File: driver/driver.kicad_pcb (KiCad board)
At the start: 2 copper layers, 59 parts, among them J1 BARREL_JACK, J2 CONN_02X32, Q1 DUAL_NPN_MOSFET, Q10 DUAL_NPN_MOSFET, Q11 DUAL_NPN_MOSFET, Q12 DUAL_NPN_MOSFET, Q13 DUAL_NPN_MOSFET, Q14 DUAL_NPN_MOSFET, Q15 DUAL_NPN_MOSFET, Q16 DUAL_NPN_MOSFET, Q17 DUAL_NPN_MOSFET, Q18 DUAL_NPN_MOSFET, Q19 DUAL_NPN_MOSFET, Q2 DUAL_NPN_MOSFET, Q20 DUAL_NPN_MOSFET, Q21 DUAL_NPN_MOSFET, Q22 DUAL_NPN_MOSFET, Q23 DUAL_NPN_MOSFET, Q24 DUAL_NPN_MOSFET, Q25 DUAL_NPN_MOSFET, Q26 DUAL_NPN_MOSFET, Q27 DUAL_NPN_MOSFET, Q28 DUAL_NPN_MOSFET, Q29 DUAL_NPN_MOSFET, Q3 DUAL_NPN_MOSFET, Q30 DUAL_NPN_MOSFET, Q31 DUAL_NPN_MOSFET, Q32 DUAL_NPN_MOSFET, Q33 DUAL_NPN_MOSFET, Q34 DUAL_NPN_MOSFET, Q35 DUAL_NPN_MOSFET, Q36 DUAL_NPN_MOSFET, Q37 DUAL_NPN_MOSFET, Q38 DUAL_NPN_MOSFET, Q39 DUAL_NPN_MOSFET, Q4 DUAL_NPN_MOSFET, Q40 DUAL_NPN_MOSFET, Q41 DUAL_NPN_MOSFET, Q42 DUAL_NPN_MOSFET, Q43 DUAL_NPN_MOSFET, Q44 DUAL_NPN_MOSFET, Q5 DUAL_NPN_MOSFET, Q6 DUAL_NPN_MOSFET, Q7 DUAL_NPN_MOSFET, Q8 DUAL_NPN_MOSFET, Q9 DUAL_NPN_MOSFET, U1 MCP23017, U2 Teensy3.2, U3 MCP23017, U4 LM7815CT, U5 MCP23017, U6 LF50ABDT-TR, U7 MCP23017, U8 MCP23017, U9 MCP23017

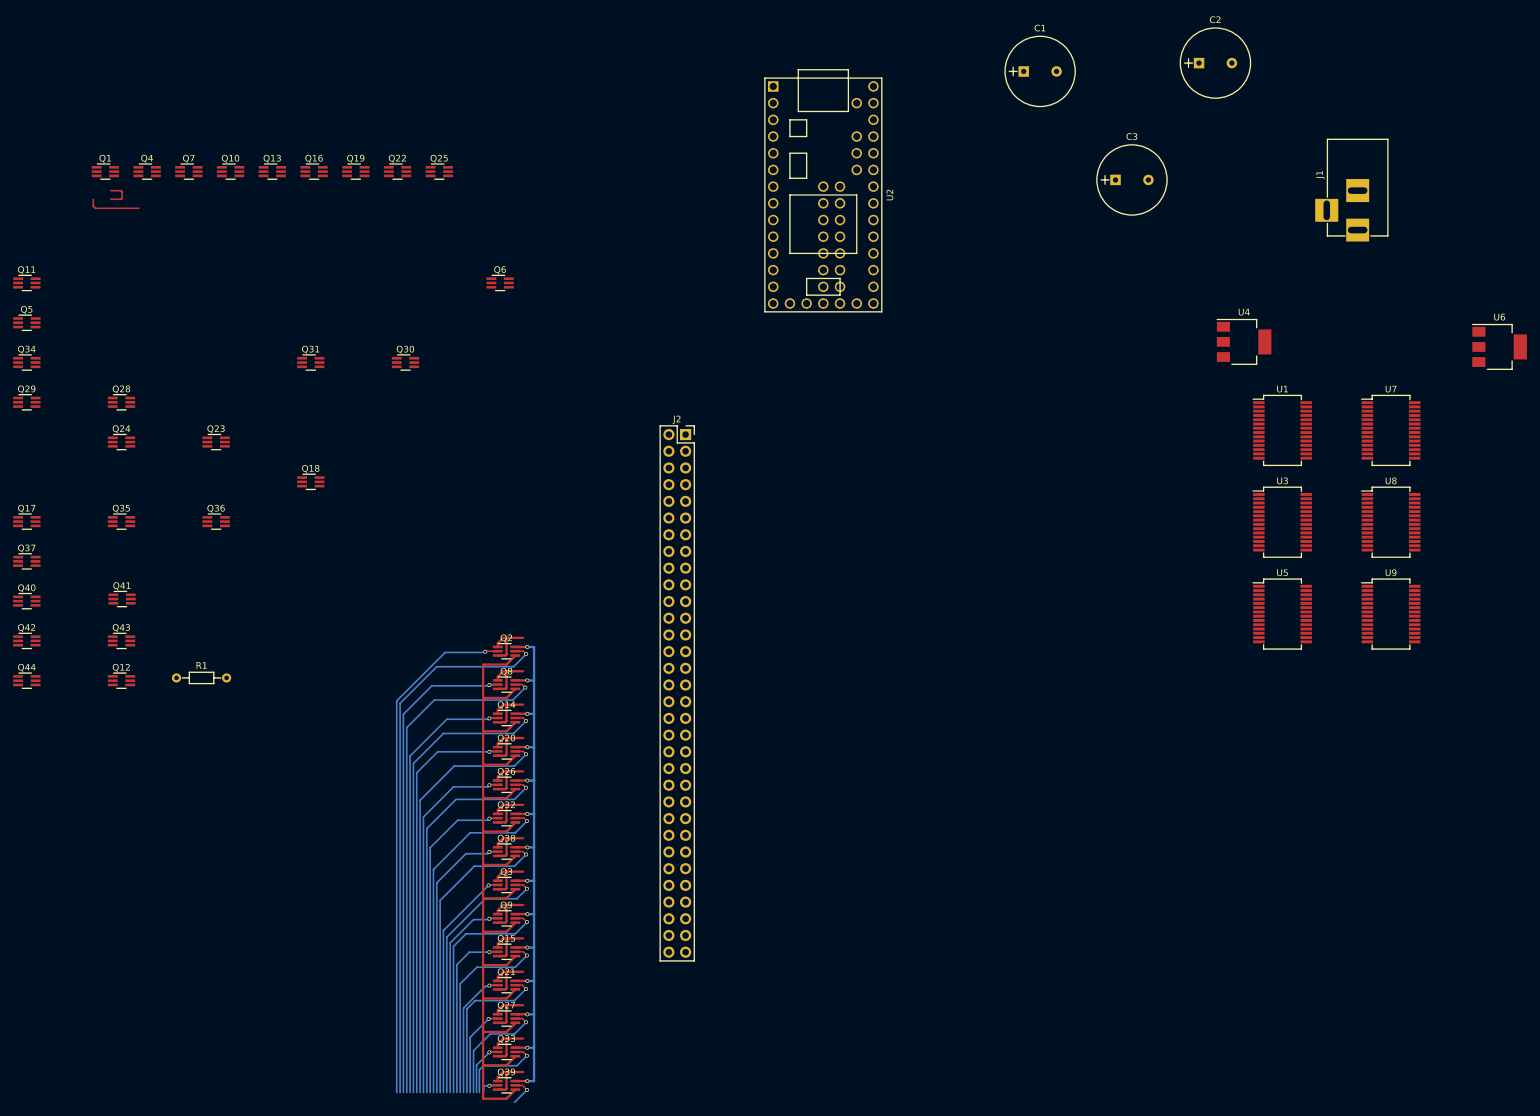
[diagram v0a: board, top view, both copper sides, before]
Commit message: layout 2nd transistor array
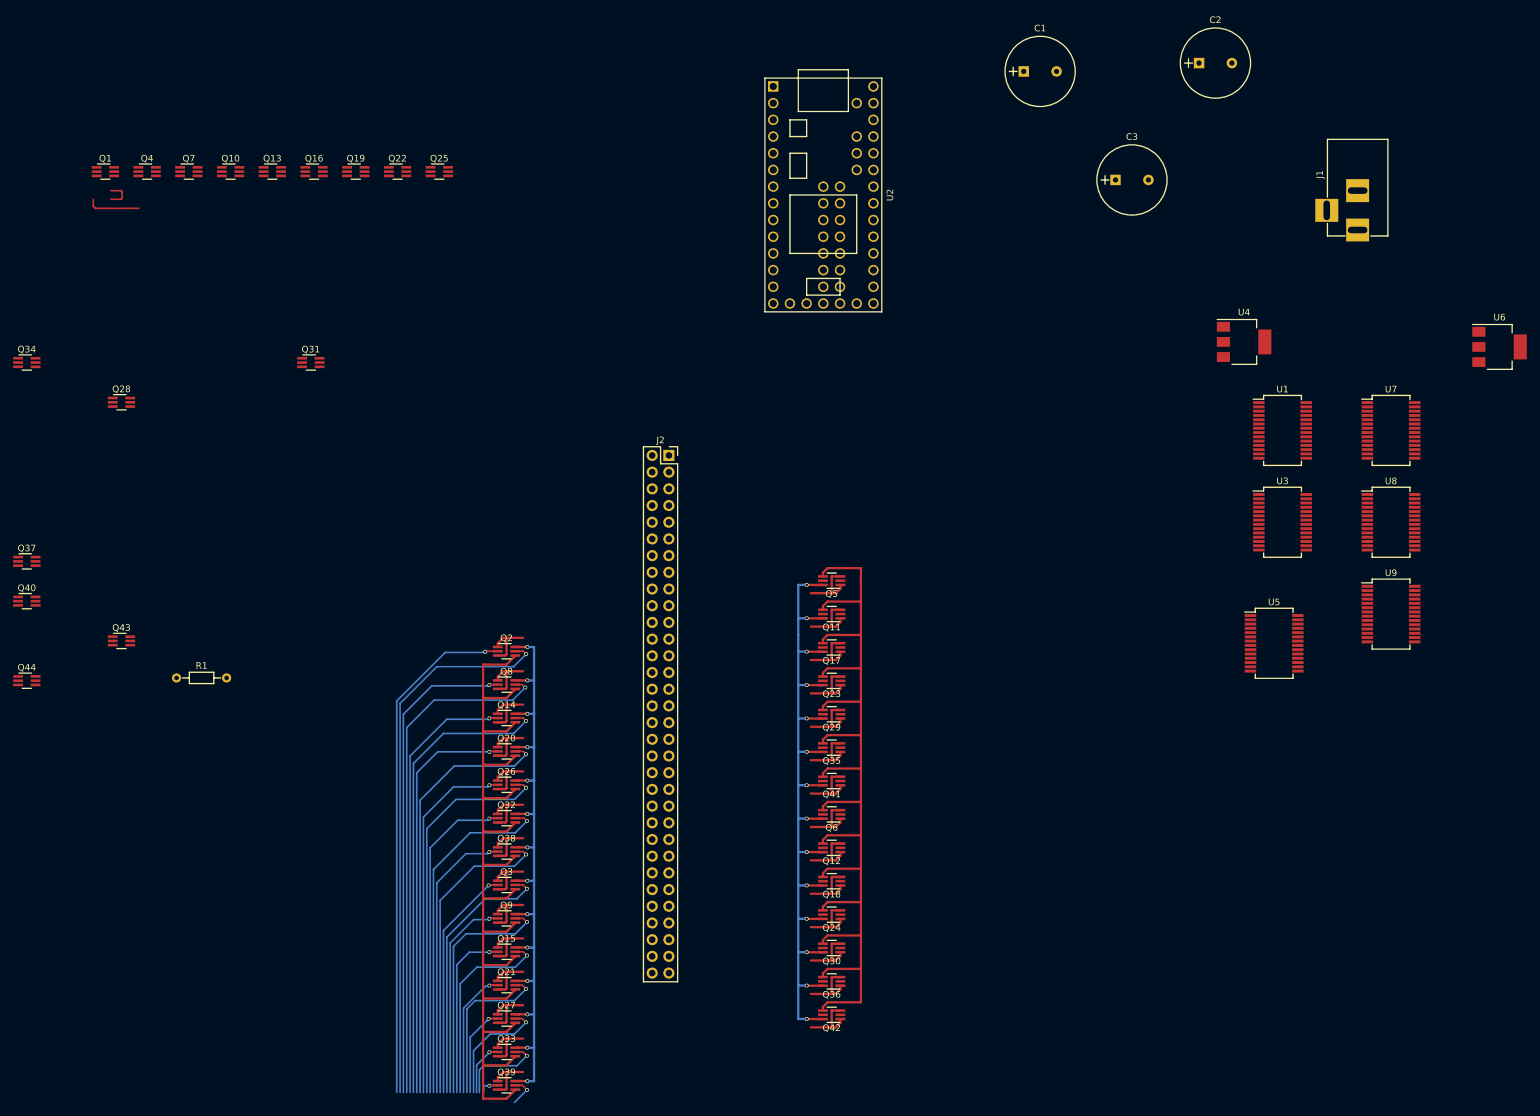
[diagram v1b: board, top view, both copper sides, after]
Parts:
- moved Q42 135.0 mm to (171.4, 168.9), turned to 180 degrees
- moved Q11 132.4 mm to (171.4, 108.0), turned to 180 degrees
- moved Q29 131.3 mm to (171.4, 123.2), turned to 180 degrees
- moved Q24 129.8 mm to (171.4, 153.7), turned to 180 degrees
- moved Q5 128.6 mm to (171.4, 102.9), turned to 180 degrees
- moved Q17 123.9 mm to (171.4, 113.0), turned to 180 degrees
- moved Q36 116.9 mm to (171.4, 163.8), turned to 180 degrees
- moved Q35 113.4 mm to (171.4, 128.3), turned to 180 degrees
- moved Q41 111.4 mm to (171.4, 133.3), turned to 180 degrees
- moved Q12 111.0 mm to (171.4, 143.5), turned to 180 degrees
- moved Q30 110.2 mm to (171.4, 158.8), turned to 180 degrees
- moved Q23 100.4 mm to (171.4, 118.1), turned to 180 degrees
- moved Q18 99.9 mm to (171.4, 148.6), turned to 180 degrees
- moved Q6 95.3 mm to (171.4, 138.4), turned to 180 degrees
- moved U5 4.62 mm to (238.8, 112.4)
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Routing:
- net /flipdot_matrix/FLIP+: track 142.9 -> 301.6 mm
- net GND: track 106.7 -> 225.3 mm, vias 14 -> 28
- net /flipdot_matrix/COL26: track 0.00 -> 9.23 mm
- net /flipdot_matrix/COL12: track 0.00 -> 9.23 mm
- net /flipdot_matrix/COL4: track 0.00 -> 9.23 mm
- net /flipdot_matrix/COL2: track 0.00 -> 9.23 mm
- net /flipdot_matrix/COL8: track 0.00 -> 9.23 mm
- net /flipdot_matrix/COL6: track 0.00 -> 9.23 mm
- net /flipdot_matrix/COL28: track 0.00 -> 9.23 mm
- net /flipdot_matrix/COL24: track 0.00 -> 9.23 mm
- net /flipdot_matrix/COL20: track 0.00 -> 9.23 mm
- net /flipdot_matrix/COL14: track 0.00 -> 9.23 mm
- net /flipdot_matrix/COL16: track 0.00 -> 9.23 mm
- net /flipdot_matrix/COL10: track 0.00 -> 9.23 mm
- net /flipdot_matrix/COL22: track 0.00 -> 9.23 mm
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
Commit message: Better row pins
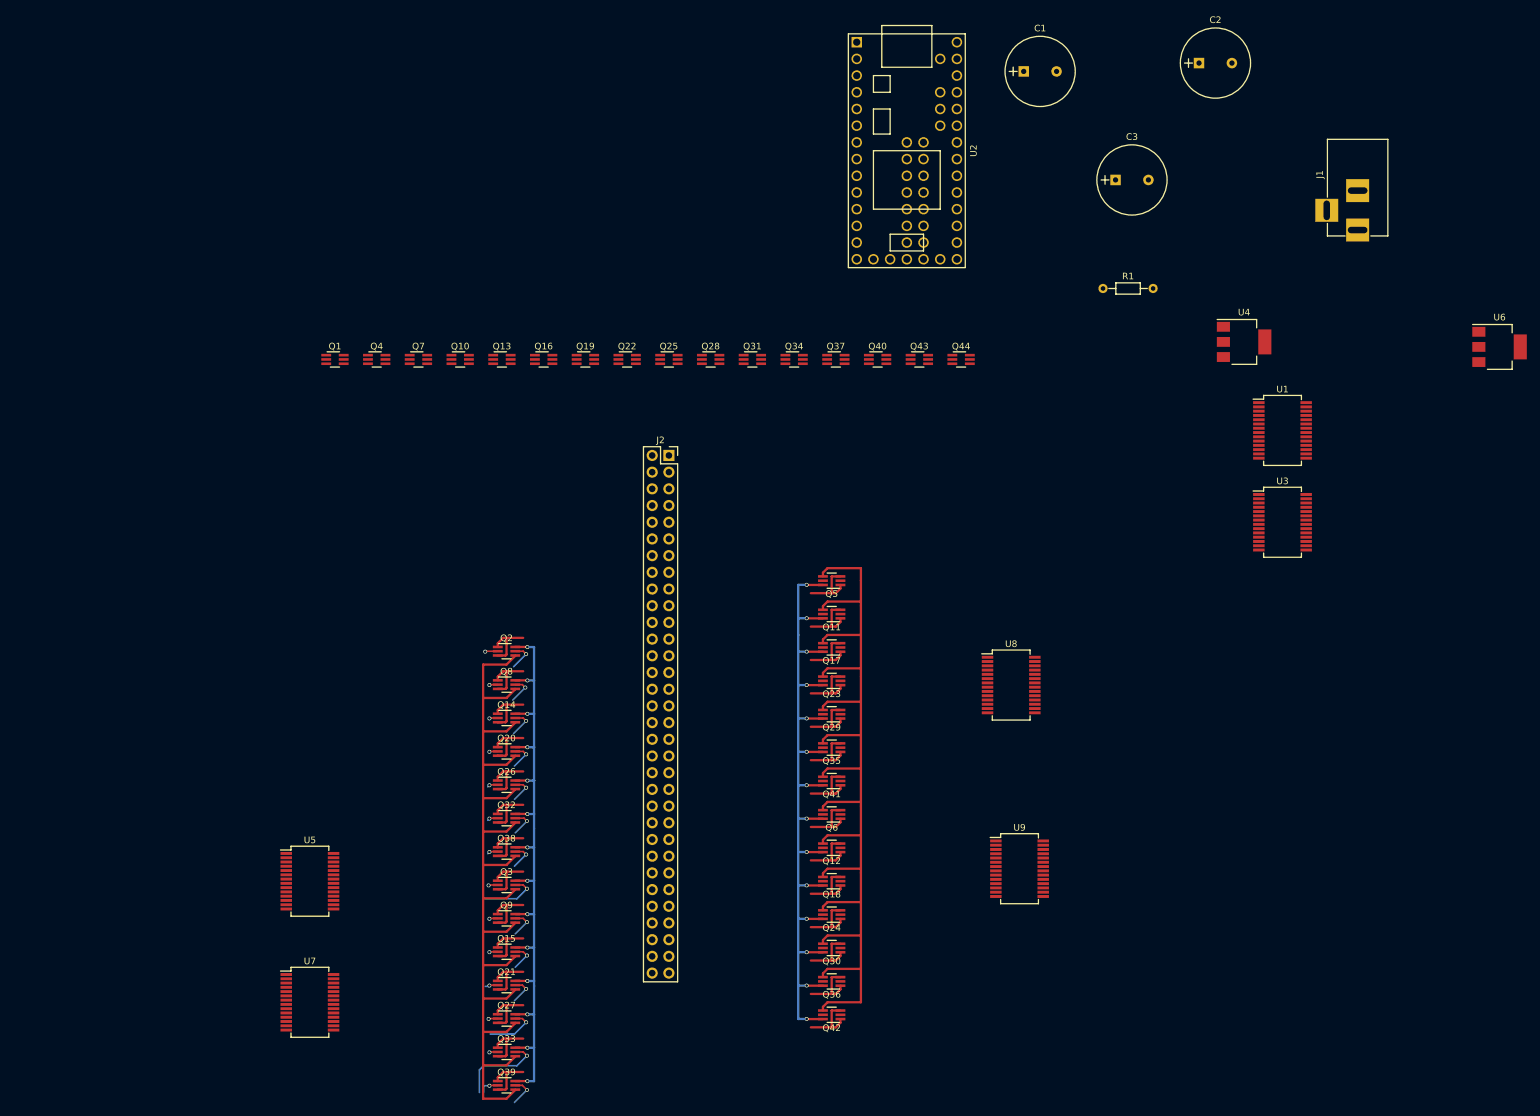
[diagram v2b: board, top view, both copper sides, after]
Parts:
- moved U7 186.1 mm to (92.1, 167.0)
- moved R1 152.9 mm to (212.7, 58.4)
- moved U5 151.1 mm to (92.1, 148.6)
- moved Q44 150.3 mm to (191.1, 69.2)
- moved Q40 134.5 mm to (178.4, 69.2)
- moved Q43 128.7 mm to (184.8, 69.2)
- moved Q37 126.9 mm to (172.1, 69.2)
- moved Q34 116.7 mm to (165.7, 69.2)
- moved Q28 89.9 mm to (153.0, 69.2)
- moved U9 68.5 mm to (200.0, 146.7)
- moved Q31 67.2 mm to (159.4, 69.2)
- moved U8 62.9 mm to (198.8, 118.7)
- moved Q16 45.1 mm to (127.6, 69.2)
- moved Q19 45.1 mm to (134.0, 69.2)
- moved Q22 45.1 mm to (140.3, 69.2)
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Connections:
- Q1 pad 1: GND -> /flipdot_matrix/FLIP+
- Q1 pad 2: /flipdot_matrix/ROW1- -> /flipdot_matrix/ROW16+
- Q1 pad 3: /flipdot_matrix/FLIP+ -> /flipdot_matrix/R16+
- Q1 pad 4: /flipdot_matrix/R1- -> /flipdot_matrix/R14+
- Q1 pad 5: /flipdot_matrix/ROW1+ -> /flipdot_matrix/ROW14+
- Q1 pad 6: /flipdot_matrix/R1+ -> /flipdot_matrix/FLIP+
- Q10 pad 1: GND -> /flipdot_matrix/FLIP+
- Q10 pad 2: /flipdot_matrix/ROW4- -> /flipdot_matrix/ROW4+
- Q10 pad 3: /flipdot_matrix/FLIP+ -> /flipdot_matrix/R4+
- Q10 pad 4: /flipdot_matrix/R4- -> /flipdot_matrix/R2+
- Q10 pad 5: /flipdot_matrix/ROW4+ -> /flipdot_matrix/ROW2+
- Q10 pad 6: /flipdot_matrix/R4+ -> /flipdot_matrix/FLIP+
- Q13 pad 1: GND -> /flipdot_matrix/FLIP+
- Q13 pad 2: /flipdot_matrix/ROW5- -> /flipdot_matrix/ROW1+
- Q13 pad 3: /flipdot_matrix/FLIP+ -> /flipdot_matrix/R1+
- Q13 pad 4: /flipdot_matrix/R5- -> /flipdot_matrix/R3+
- Q13 pad 5: /flipdot_matrix/ROW5+ -> /flipdot_matrix/ROW3+
- Q13 pad 6: /flipdot_matrix/R5+ -> /flipdot_matrix/FLIP+
- Q16 pad 1: GND -> /flipdot_matrix/FLIP+
- Q16 pad 2: /flipdot_matrix/ROW6- -> /flipdot_matrix/ROW5+
- Q16 pad 3: /flipdot_matrix/FLIP+ -> /flipdot_matrix/R5+
- Q16 pad 4: /flipdot_matrix/R6- -> /flipdot_matrix/R7+
- Q16 pad 5: /flipdot_matrix/ROW6+ -> /flipdot_matrix/ROW7+
- Q16 pad 6: /flipdot_matrix/R6+ -> /flipdot_matrix/FLIP+
- Q19 pad 1: GND -> /flipdot_matrix/FLIP+
- Q19 pad 2: /flipdot_matrix/ROW7- -> /flipdot_matrix/ROW9+
- Q19 pad 3: /flipdot_matrix/FLIP+ -> /flipdot_matrix/R9+
- Q19 pad 4: /flipdot_matrix/R7- -> /flipdot_matrix/R11+
- Q19 pad 5: /flipdot_matrix/ROW7+ -> /flipdot_matrix/ROW11+
- Q19 pad 6: /flipdot_matrix/R7+ -> /flipdot_matrix/FLIP+
- Q22 pad 1: GND -> /flipdot_matrix/FLIP+
- Q22 pad 2: /flipdot_matrix/ROW8- -> /flipdot_matrix/ROW13+
- Q22 pad 3: /flipdot_matrix/FLIP+ -> /flipdot_matrix/R13+
- Q22 pad 4: /flipdot_matrix/R8- -> /flipdot_matrix/R15+
- Q22 pad 5: /flipdot_matrix/ROW8+ -> /flipdot_matrix/ROW15+
- Q22 pad 6: /flipdot_matrix/R8+ -> /flipdot_matrix/FLIP+
- Q25 pad 1: GND -> /flipdot_matrix/R16-
- Q25 pad 2: /flipdot_matrix/ROW9- -> /flipdot_matrix/ROW16-
- Q25 pad 3: /flipdot_matrix/FLIP+ -> GND
- Q25 pad 4: /flipdot_matrix/R9- -> GND
- Q25 pad 5: /flipdot_matrix/ROW9+ -> /flipdot_matrix/ROW14-
- Q25 pad 6: /flipdot_matrix/R9+ -> /flipdot_matrix/R14-
- Q28 pad 1: GND -> /flipdot_matrix/R12-
- Q28 pad 2: /flipdot_matrix/ROW10- -> /flipdot_matrix/ROW12-
- Q28 pad 3: /flipdot_matrix/FLIP+ -> GND
- Q28 pad 4: /flipdot_matrix/R10- -> GND
- Q28 pad 5: /flipdot_matrix/ROW10+ -> /flipdot_matrix/ROW10-
- Q28 pad 6: /flipdot_matrix/R10+ -> /flipdot_matrix/R10-
- Q31 pad 1: GND -> /flipdot_matrix/R8-
- Q31 pad 2: /flipdot_matrix/ROW11- -> /flipdot_matrix/ROW8-
- Q31 pad 3: /flipdot_matrix/FLIP+ -> GND
- Q31 pad 4: /flipdot_matrix/R11- -> GND
- Q31 pad 5: /flipdot_matrix/ROW11+ -> /flipdot_matrix/ROW6-
- Q31 pad 6: /flipdot_matrix/R11+ -> /flipdot_matrix/R6-
- Q34 pad 1: GND -> /flipdot_matrix/R4-
- Q34 pad 2: /flipdot_matrix/ROW12- -> /flipdot_matrix/ROW4-
- Q34 pad 3: /flipdot_matrix/FLIP+ -> GND
- Q34 pad 4: /flipdot_matrix/R12- -> GND
- Q34 pad 5: /flipdot_matrix/ROW12+ -> /flipdot_matrix/ROW2-
- Q34 pad 6: /flipdot_matrix/R12+ -> /flipdot_matrix/R2-
- Q37 pad 1: GND -> /flipdot_matrix/R1-
- Q37 pad 2: /flipdot_matrix/ROW13- -> /flipdot_matrix/ROW1-
- Q37 pad 3: /flipdot_matrix/FLIP+ -> GND
- Q37 pad 4: /flipdot_matrix/R13- -> GND
- Q37 pad 5: /flipdot_matrix/ROW13+ -> /flipdot_matrix/ROW3-
- Q37 pad 6: /flipdot_matrix/R13+ -> /flipdot_matrix/R3-
- Q4 pad 1: GND -> /flipdot_matrix/FLIP+
- Q4 pad 2: /flipdot_matrix/ROW2- -> /flipdot_matrix/ROW12+
- Q4 pad 3: /flipdot_matrix/FLIP+ -> /flipdot_matrix/R12+
- Q4 pad 4: /flipdot_matrix/R2- -> /flipdot_matrix/R10+
- Q4 pad 5: /flipdot_matrix/ROW2+ -> /flipdot_matrix/ROW10+
- Q4 pad 6: /flipdot_matrix/R2+ -> /flipdot_matrix/FLIP+
- Q40 pad 1: GND -> /flipdot_matrix/R5-
- Q40 pad 2: /flipdot_matrix/ROW14- -> /flipdot_matrix/ROW5-
- Q40 pad 3: /flipdot_matrix/FLIP+ -> GND
- Q40 pad 4: /flipdot_matrix/R14- -> GND
- Q40 pad 5: /flipdot_matrix/ROW14+ -> /flipdot_matrix/ROW7-
- Q40 pad 6: /flipdot_matrix/R14+ -> /flipdot_matrix/R7-
- Q43 pad 1: GND -> /flipdot_matrix/R9-
- Q43 pad 2: /flipdot_matrix/ROW15- -> /flipdot_matrix/ROW9-
- Q43 pad 3: /flipdot_matrix/FLIP+ -> GND
- Q43 pad 4: /flipdot_matrix/R15- -> GND
- Q43 pad 5: /flipdot_matrix/ROW15+ -> /flipdot_matrix/ROW11-
- Q43 pad 6: /flipdot_matrix/R15+ -> /flipdot_matrix/R11-
- Q44 pad 1: GND -> /flipdot_matrix/R13-
- Q44 pad 2: /flipdot_matrix/ROW16- -> /flipdot_matrix/ROW13-
- Q44 pad 3: /flipdot_matrix/FLIP+ -> GND
- Q44 pad 4: /flipdot_matrix/R16- -> GND
- Q44 pad 5: /flipdot_matrix/ROW16+ -> /flipdot_matrix/ROW15-
- Q44 pad 6: /flipdot_matrix/R16+ -> /flipdot_matrix/R15-
- Q7 pad 1: GND -> /flipdot_matrix/FLIP+
- Q7 pad 2: /flipdot_matrix/ROW3- -> /flipdot_matrix/ROW8+
- Q7 pad 3: /flipdot_matrix/FLIP+ -> /flipdot_matrix/R8+
- Q7 pad 4: /flipdot_matrix/R3- -> /flipdot_matrix/R6+
- Q7 pad 5: /flipdot_matrix/ROW3+ -> /flipdot_matrix/ROW6+
- Q7 pad 6: /flipdot_matrix/R3+ -> /flipdot_matrix/FLIP+
- U5 pad 21: /flipdot_matrix/COL5+ -> /flipdot_matrix/COL9+
- U5 pad 22: /flipdot_matrix/COL5- -> /flipdot_matrix/COL9-
- U5 pad 23: /flipdot_matrix/COL6+ -> /flipdot_matrix/COL11+
- U5 pad 24: /flipdot_matrix/COL6- -> /flipdot_matrix/COL11-
- U5 pad 25: /flipdot_matrix/COL7+ -> /flipdot_matrix/COL13+
- U5 pad 26: /flipdot_matrix/COL7- -> /flipdot_matrix/COL13-
- U5 pad 27: /flipdot_matrix/COL8+ -> /flipdot_matrix/COL15+
- U5 pad 28: /flipdot_matrix/COL8- -> /flipdot_matrix/COL15-
- U5 pad 3: /flipdot_matrix/COL2+ -> /flipdot_matrix/COL3+
- U5 pad 4: /flipdot_matrix/COL2- -> /flipdot_matrix/COL3-
- U5 pad 5: /flipdot_matrix/COL3+ -> /flipdot_matrix/COL5+
- U5 pad 6: /flipdot_matrix/COL3- -> /flipdot_matrix/COL5-
- U5 pad 7: /flipdot_matrix/COL4+ -> /flipdot_matrix/COL7+
- U5 pad 8: /flipdot_matrix/COL4- -> /flipdot_matrix/COL7-
- U7 pad 1: /flipdot_matrix/COL9+ -> /flipdot_matrix/COL17+
- U7 pad 2: /flipdot_matrix/COL9- -> /flipdot_matrix/COL17-
- U7 pad 21: /flipdot_matrix/COL13+ -> /flipdot_matrix/COL25+
- U7 pad 22: /flipdot_matrix/COL13- -> /flipdot_matrix/COL25-
- U7 pad 23: /flipdot_matrix/COL14+ -> /flipdot_matrix/COL27+
- U7 pad 24: /flipdot_matrix/COL14- -> /flipdot_matrix/COL27-
- U7 pad 25: /flipdot_matrix/COL15+ -> Net-(U7-Pad25)
- U7 pad 26: /flipdot_matrix/COL15- -> Net-(U7-Pad26)
- U7 pad 27: /flipdot_matrix/COL16+ -> Net-(U7-Pad27)
- U7 pad 28: /flipdot_matrix/COL16- -> Net-(U7-Pad28)
- U7 pad 3: /flipdot_matrix/COL10+ -> /flipdot_matrix/COL19+
- U7 pad 4: /flipdot_matrix/COL10- -> /flipdot_matrix/COL19-
- U7 pad 5: /flipdot_matrix/COL11+ -> /flipdot_matrix/COL21+
- U7 pad 6: /flipdot_matrix/COL11- -> /flipdot_matrix/COL21-
- U7 pad 7: /flipdot_matrix/COL12+ -> /flipdot_matrix/COL23+
- U7 pad 8: /flipdot_matrix/COL12- -> /flipdot_matrix/COL23-
- U8 pad 1: /flipdot_matrix/COL17+ -> /flipdot_matrix/COL2+
- U8 pad 2: /flipdot_matrix/COL17- -> /flipdot_matrix/COL2-
- U8 pad 21: /flipdot_matrix/COL21+ -> /flipdot_matrix/COL10+
- U8 pad 22: /flipdot_matrix/COL21- -> /flipdot_matrix/COL10-
- U8 pad 23: /flipdot_matrix/COL22+ -> /flipdot_matrix/COL12+
- U8 pad 24: /flipdot_matrix/COL22- -> /flipdot_matrix/COL12-
- U8 pad 25: /flipdot_matrix/COL23+ -> /flipdot_matrix/COL14+
- U8 pad 26: /flipdot_matrix/COL23- -> /flipdot_matrix/COL14-
- U8 pad 27: /flipdot_matrix/COL24+ -> /flipdot_matrix/COL16+
- U8 pad 28: /flipdot_matrix/COL24- -> /flipdot_matrix/COL16-
- U8 pad 3: /flipdot_matrix/COL18+ -> /flipdot_matrix/COL4+
- U8 pad 4: /flipdot_matrix/COL18- -> /flipdot_matrix/COL4-
- U8 pad 5: /flipdot_matrix/COL19+ -> /flipdot_matrix/COL6+
- U8 pad 6: /flipdot_matrix/COL19- -> /flipdot_matrix/COL6-
- U8 pad 7: /flipdot_matrix/COL20+ -> /flipdot_matrix/COL8+
- U8 pad 8: /flipdot_matrix/COL20- -> /flipdot_matrix/COL8-
- U9 pad 1: /flipdot_matrix/COL25+ -> /flipdot_matrix/COL18+
- U9 pad 2: /flipdot_matrix/COL25- -> /flipdot_matrix/COL18-
- U9 pad 21: Net-(U9-Pad21) -> /flipdot_matrix/COL26+
- U9 pad 22: Net-(U9-Pad22) -> /flipdot_matrix/COL26-
- U9 pad 23: Net-(U9-Pad23) -> /flipdot_matrix/COL28+
- U9 pad 24: Net-(U9-Pad24) -> /flipdot_matrix/COL28-
- U9 pad 3: /flipdot_matrix/COL26+ -> /flipdot_matrix/COL20+
- U9 pad 4: /flipdot_matrix/COL26- -> /flipdot_matrix/COL20-
- U9 pad 5: /flipdot_matrix/COL27+ -> /flipdot_matrix/COL22+
- U9 pad 6: /flipdot_matrix/COL27- -> /flipdot_matrix/COL22-
- U9 pad 7: /flipdot_matrix/COL28+ -> /flipdot_matrix/COL24+
- U9 pad 8: /flipdot_matrix/COL28- -> /flipdot_matrix/COL24-
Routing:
- net /flipdot_matrix/COL1+: track 83.3 -> 4.53 mm
- net /flipdot_matrix/COL1-: track 78.1 -> 2.11 mm
- net /flipdot_matrix/COL3+: track 77.8 -> 4.41 mm
- net /flipdot_matrix/COL3-: track 73.8 -> 1.48 mm
- net /flipdot_matrix/COL5+: track 71.7 -> 4.53 mm
- net /flipdot_matrix/COL5-: track 66.9 -> 1.48 mm
- net /flipdot_matrix/COL7-: track 62.3 -> 1.30 mm
- net /flipdot_matrix/COL7+: track 65.3 -> 4.35 mm
- net /flipdot_matrix/COL9+: track 59.7 -> 4.35 mm
- net /flipdot_matrix/COL9-: track 55.2 -> 1.66 mm
- net /flipdot_matrix/COL11+: track 53.1 -> 4.48 mm
- net /flipdot_matrix/COL11-: track 49.4 -> 1.66 mm
- net /flipdot_matrix/COL13+: track 47.0 -> 4.35 mm
- net /flipdot_matrix/COL13-: track 43.1 -> 1.66 mm
- net /flipdot_matrix/COL15-: track 35.8 -> 1.43 mm
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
